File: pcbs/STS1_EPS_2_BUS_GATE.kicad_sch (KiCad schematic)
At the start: 12 parts, among them Q5 SI7135DP-T1-GE3, Q6 2N7002, U10 4072, U3 TPS2420RSAT

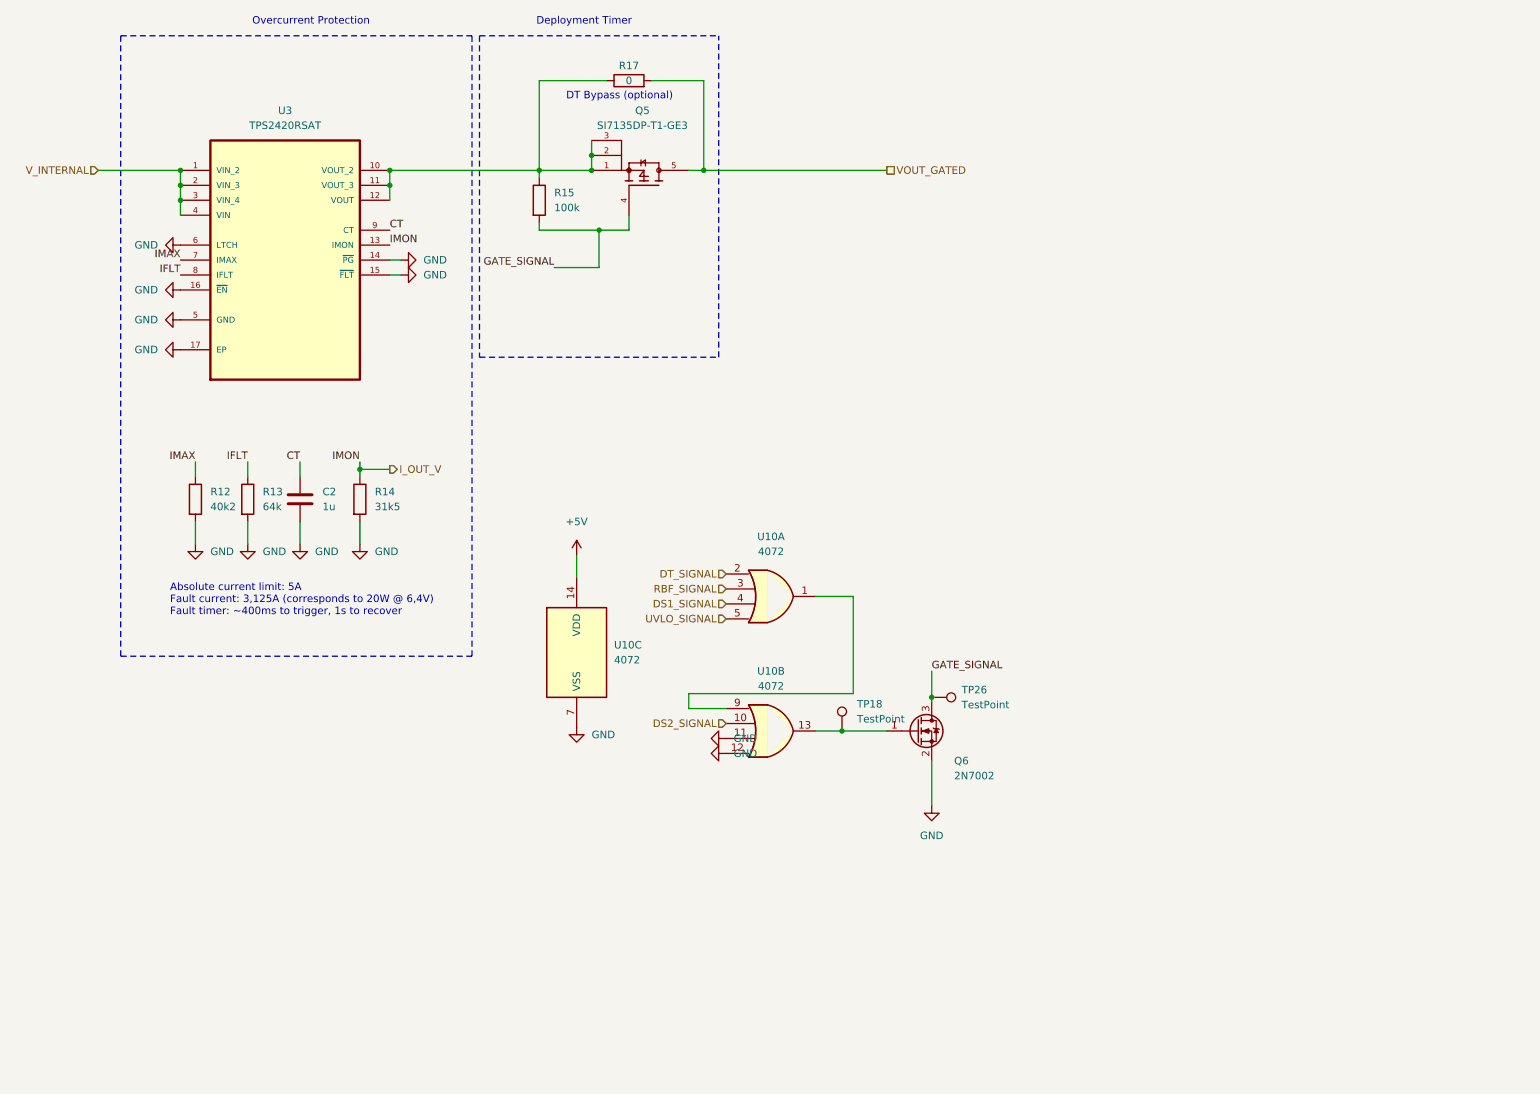
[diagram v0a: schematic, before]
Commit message: Signals to the bus gate should now be provided with supply voltage the proper way.
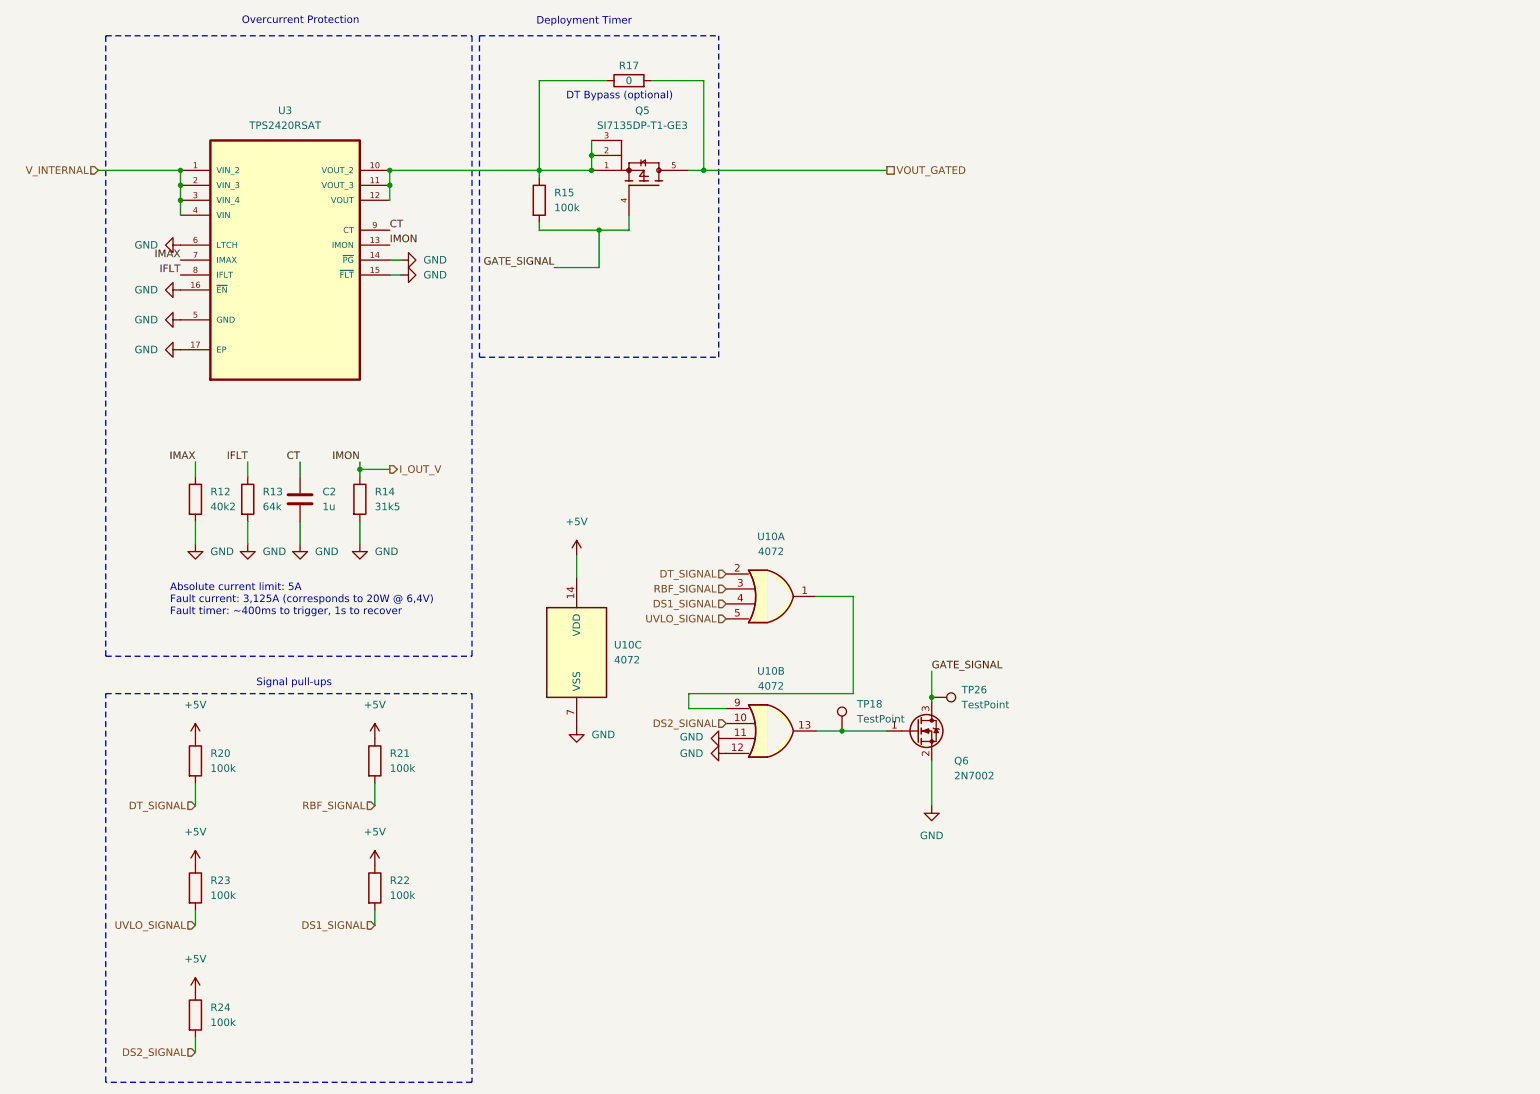
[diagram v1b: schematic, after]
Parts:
- added R20, R21, R22, R23, R24: 100k, Resistor_SMD:R_0805_2012Metric, symbol Device:R
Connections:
- net +5V: now also R20.1, R21.1, R22.1, R23.1, R24.1
- net DS1_SIGNAL: now also R22.2
- net DS2_SIGNAL: now also R24.2
- net DT_SIGNAL: now also R20.2
- net RBF_SIGNAL: now also R21.2
- net UVLO_SIGNAL: now also R23.2
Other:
- note added: "Signal pull-ups"

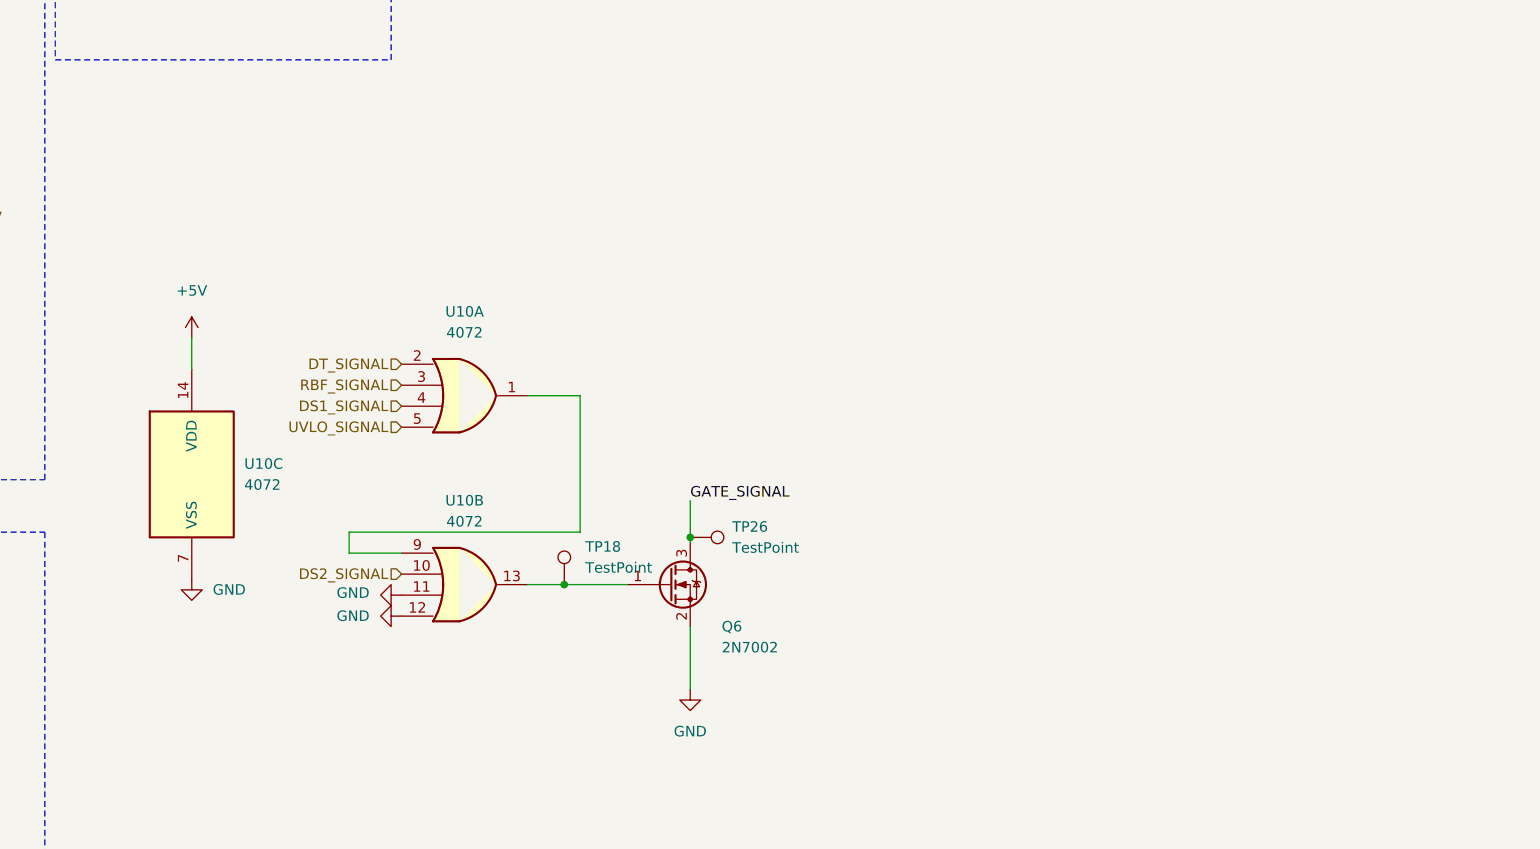
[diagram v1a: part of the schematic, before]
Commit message: Fixed the logic behing the GATE_SIGNAL signal.
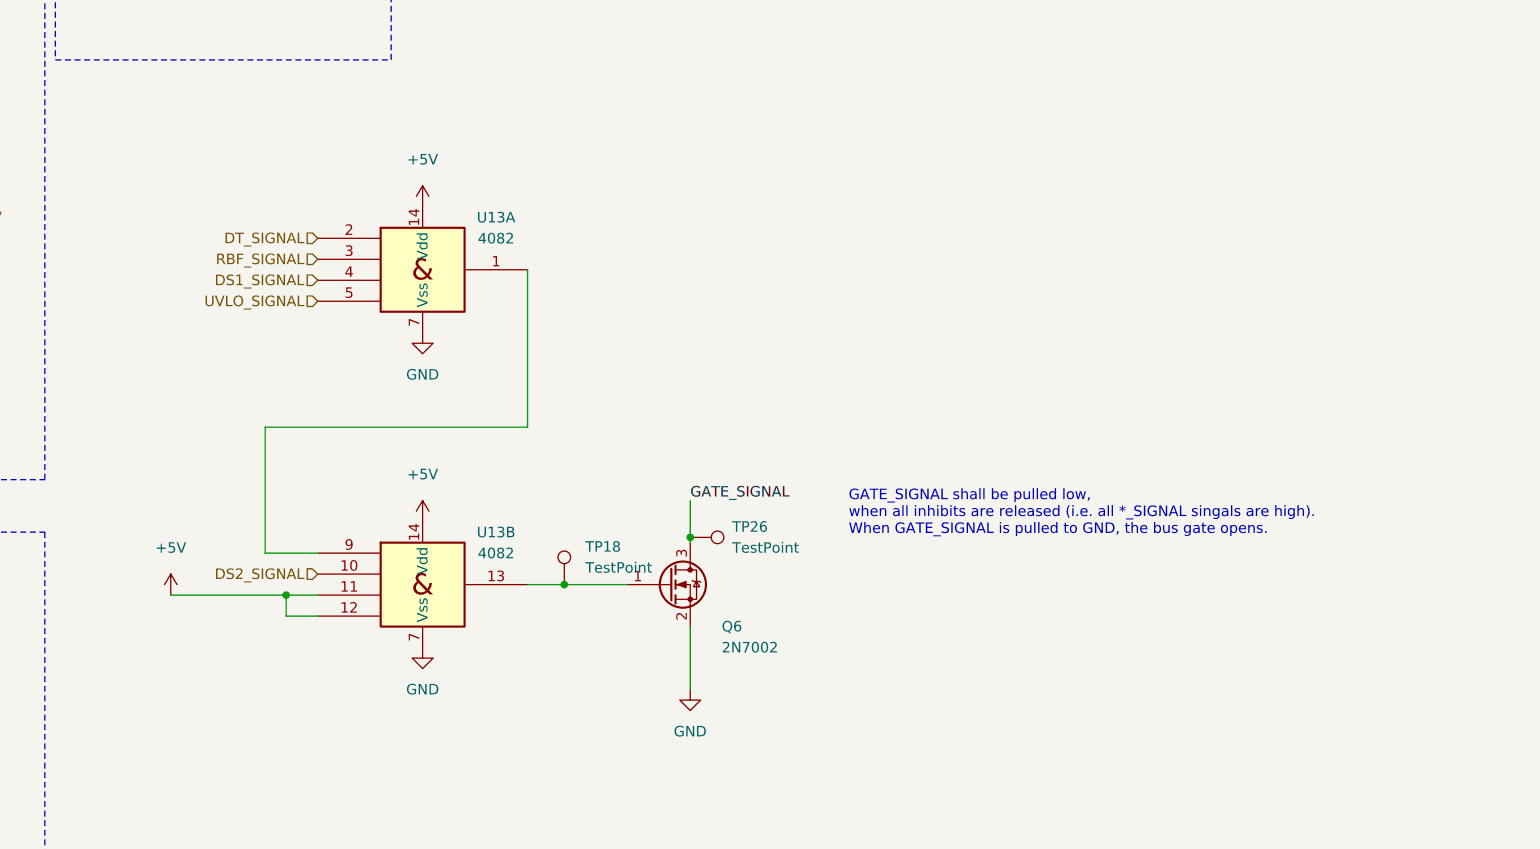
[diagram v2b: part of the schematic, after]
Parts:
- removed U10: 4072, STS_Misc:SOP127P780X200-14N, symbol 4xxx:4072
- added U13: 4082, Package_SO:SO-14_5.3x10.2mm_P1.27mm, symbol 4xxx_IEEE:4082
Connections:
- net +5V: now also U13.11, U13.12, U13.14 (Vdd), U13.14 (Vdd)
- net DS1_SIGNAL: now also U13.4
- net DS2_SIGNAL: now also U13.10
- net DT_SIGNAL: now also U13.2
- net GND: now also U13.7 (Vss), U13.7 (Vss)
- net RBF_SIGNAL: now also U13.3
- net UVLO_SIGNAL: now also U13.5
- net at Q6.1 (G), TP18.1: now also U13.13
- new net: U13.1, U13.9
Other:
- note added: "GATE_SIGNAL shall be pulled low, when all inhibits are released (i.e. all *_SIGNAL singals are high). When GATE_SIGNAL is pulled to GND, the bus gate opens."

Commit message: Intermediate commit.
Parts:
- U13: footprint Package_SO:SO-14_5.3x10.2mm_P1.27mm -> Package_SO:SOIC-14_3.9x8.7mm_P1.27mm
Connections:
- net +5V: no longer R20.1, R21.1, R22.1, R23.1, R24.1, U13.14 (Vdd), U13.14 (Vdd)
- new net V_LOGIC: R20.1, R21.1, R22.1, R23.1, R24.1, U13.14 (Vdd), U13.14 (Vdd)
